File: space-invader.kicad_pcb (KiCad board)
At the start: 2 copper layers, 95.3 x 81 mm, 35 parts, among them SW1 SW_Push, SW10 SW_Push, SW11 SW_Push, SW12 SW_Push, SW13 SW_Push, SW14 SW_Push, SW15 SW_Push, SW16 SW_Push, SW17 SW_Push, SW2 SW_Push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

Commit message: there be graphics
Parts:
- U1: footprint PCM_marbastlib-xp-promicroish:Xiao_nRF52840_ACH -> PCM_marbastlib-xp-promicroish:Xiao_nRF52840_AC_Reflow
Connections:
- U1 pad 11: unconnected-(U1-P1.15-Pad11) -> col0
- U1 pad 12: col0 -> col1
- U1 pad 13: col1 -> row0
- U1 pad 14: unconnected-(U1-P1.12-Pad14) -> row1
- U1 pad 4: row0 -> unconnected-(U1-P0.29-Pad4)
- U1 pad 5: row1 -> unconnected-(U1-P0.04-Pad5)
- U1 pad 6: col2 -> row2
- U1 pad 7: row2 -> col2
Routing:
- net row3: track 66.3 -> 100.2 mm, vias 0 -> 2
- net row1: track 124.1 -> 111.3 mm
- net col2: track 63.5 -> 73.8 mm
- net row0: track 146.5 -> 136.9 mm
- net row2: track 57.1 -> 63.5 mm
- net col4: track 82.5 -> 88.7 mm
- net col0: track 109.5 -> 110.1 mm
- net Net-(D17-A): track 20.4 -> 19.9 mm
- added copper zone on B.Cu, net (none)
- added copper zone on F.Cu, net (none)
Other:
- outline, holes or cut-outs redrawn

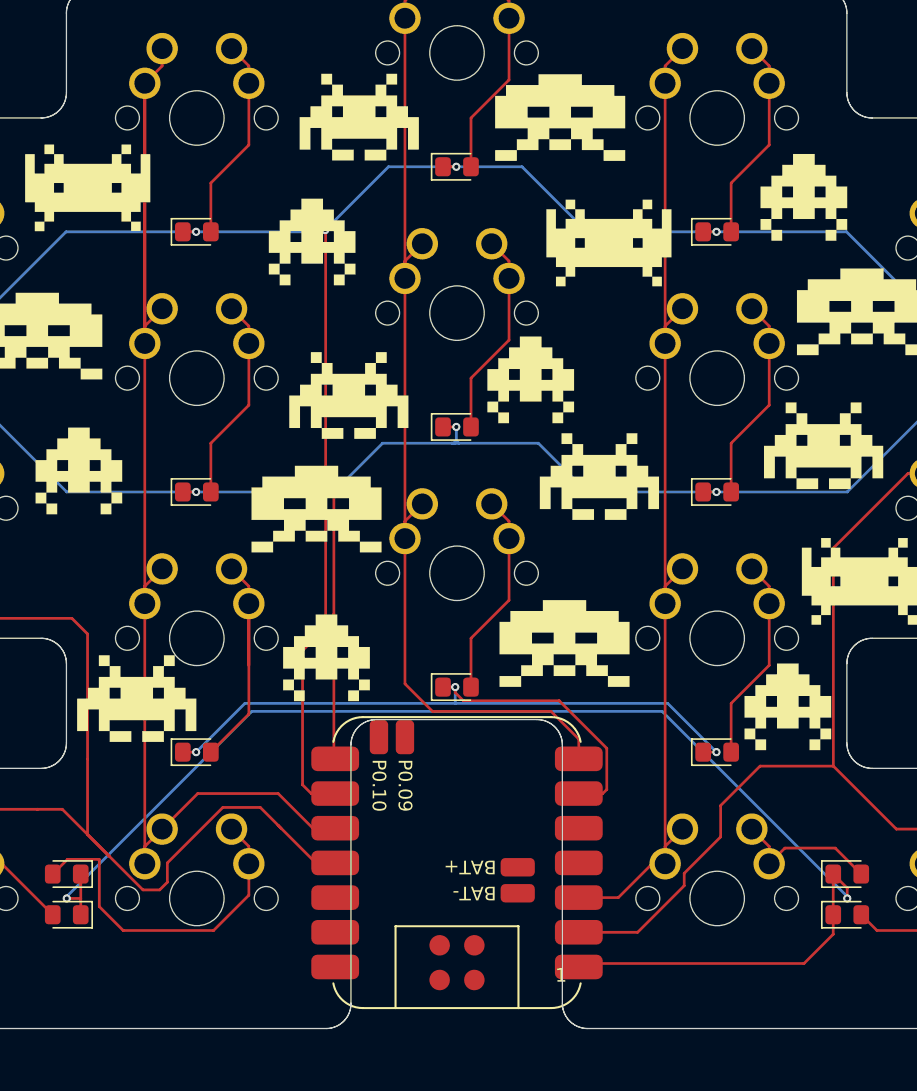
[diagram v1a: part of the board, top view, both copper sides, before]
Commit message: flipped XIAO upside down
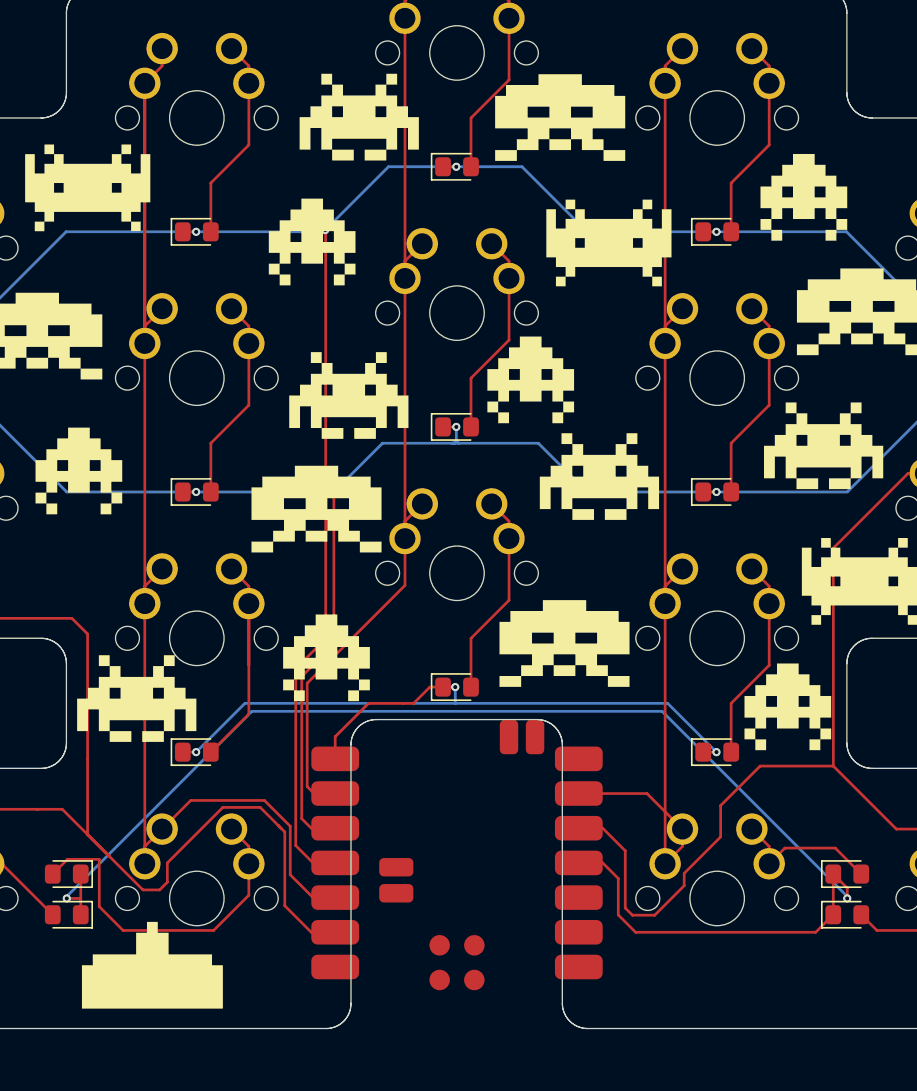
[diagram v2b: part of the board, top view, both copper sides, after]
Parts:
- added kibuzzard-67AF24A7: G***, kibuzzard-67AF24A7, B.Cu at (80.0, 94.5)
- added kibuzzard-67AF24D7: G***, kibuzzard-67AF24D7, B.Cu at (66.7, 97.7)
- added kibuzzard-67AF254E: G***, kibuzzard-67AF254E, B.Cu at (141.4, 94.4)
- added kibuzzard-67AF2568: G***, kibuzzard-67AF2568, B.Cu at (125.3, 97.9)
- U1: footprint PCM_marbastlib-xp-promicroish:Xiao_nRF52840_AC_Reflow -> PCM_marbastlib-xp-promicroish:Xiao_nRF52840_AC_Reflow_invert; moved to B.Cu
- turned U1 to 0 degrees
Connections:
- U1 pad 1: row3 -> unconnected-(U1-P0.02-Pad1)
- U1 pad 11: col0 -> row3
- U1 pad 12: col1 -> col4
- U1 pad 13: row0 -> col3
- U1 pad 14: row1 -> unconnected-(U1-P1.12-Pad14)
- U1 pad 2: col4 -> col0
- U1 pad 3: col3 -> col1
- U1 pad 4: unconnected-(U1-P0.29-Pad4) -> row0
- U1 pad 5: unconnected-(U1-P0.04-Pad5) -> row1
- U1 pad 6: row2 -> col2
- U1 pad 7: col2 -> row2
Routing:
- net row1: track 111.3 -> 119.4 mm
- net row2: track 63.5 -> 56.3 mm
- net row0: track 136.9 -> 142.3 mm
- net col0: track 110.1 -> 114.8 mm
- net col4: track 88.7 -> 93.2 mm
- net col1: track 103.3 -> 107.0 mm
- net col2: track 73.8 -> 70.7 mm
- net row3: track 100.2 -> 100.8 mm
